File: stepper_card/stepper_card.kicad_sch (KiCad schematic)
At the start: 19 parts, among them J1 Bus_PCI_Express_x1, J2 Conn_01x04, SW1 SW_DIP_x04, U1 DRV8825PWPR_Stepper_Driver

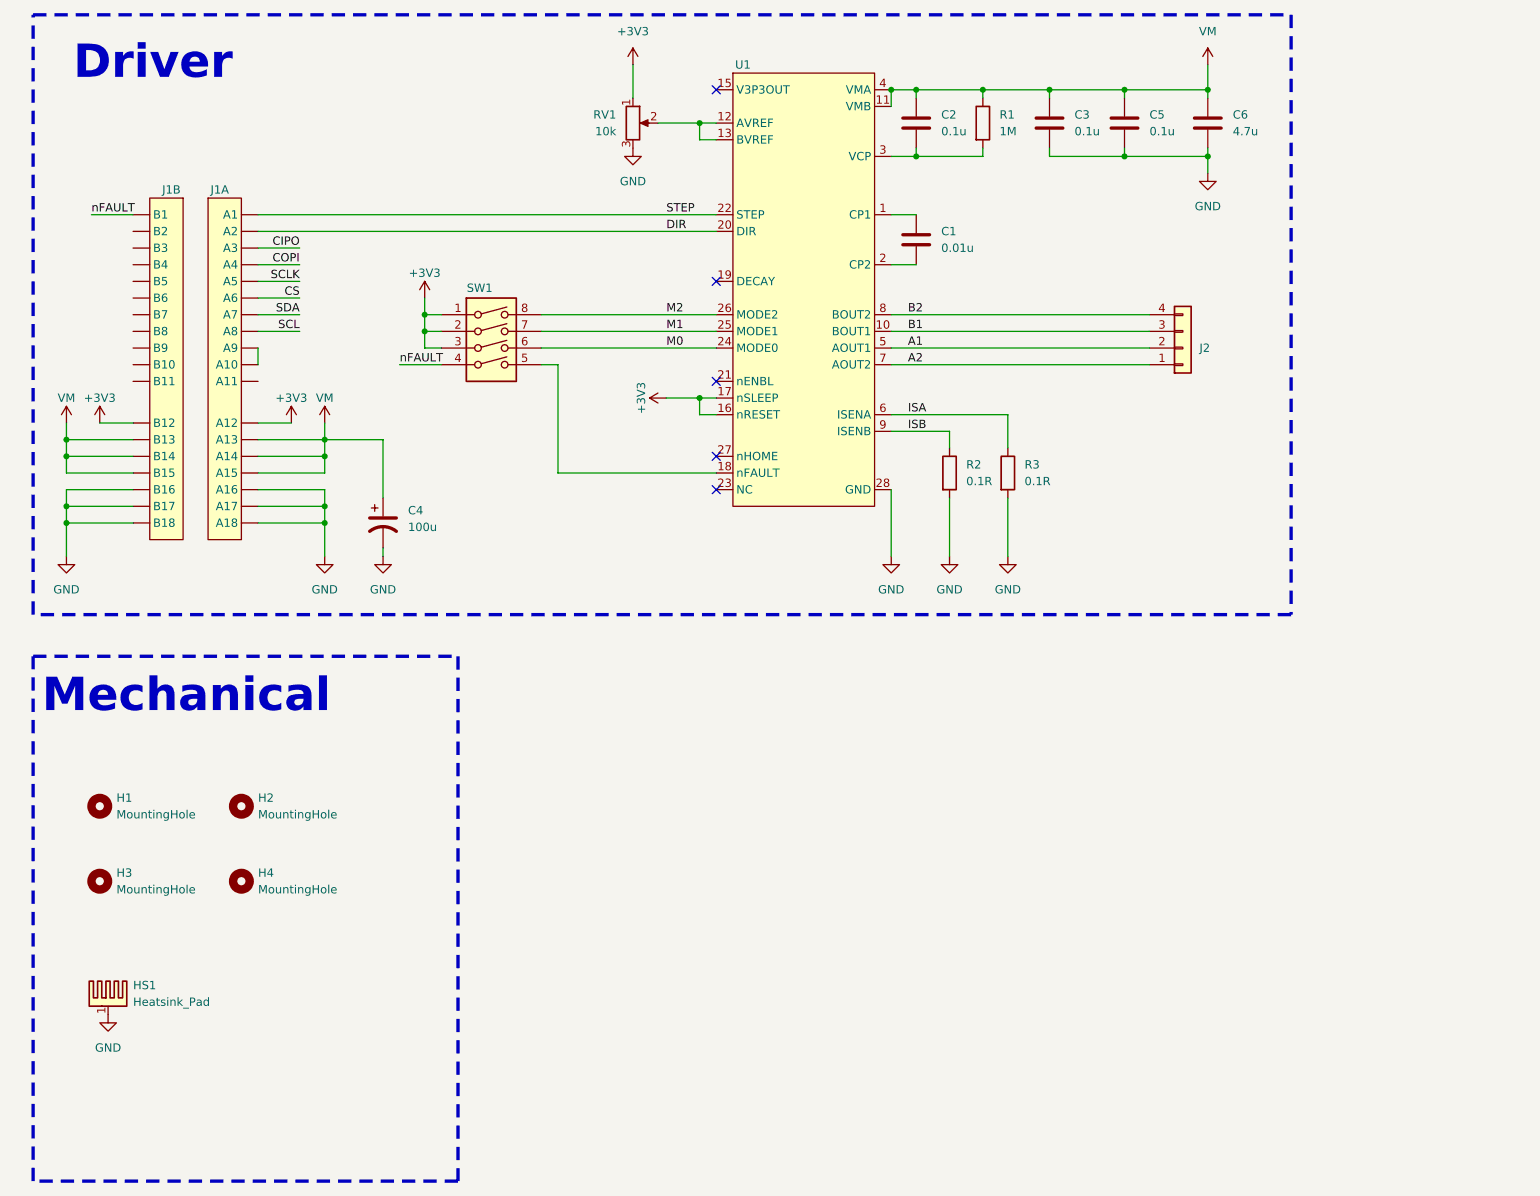
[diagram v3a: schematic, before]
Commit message: finished routing added test points
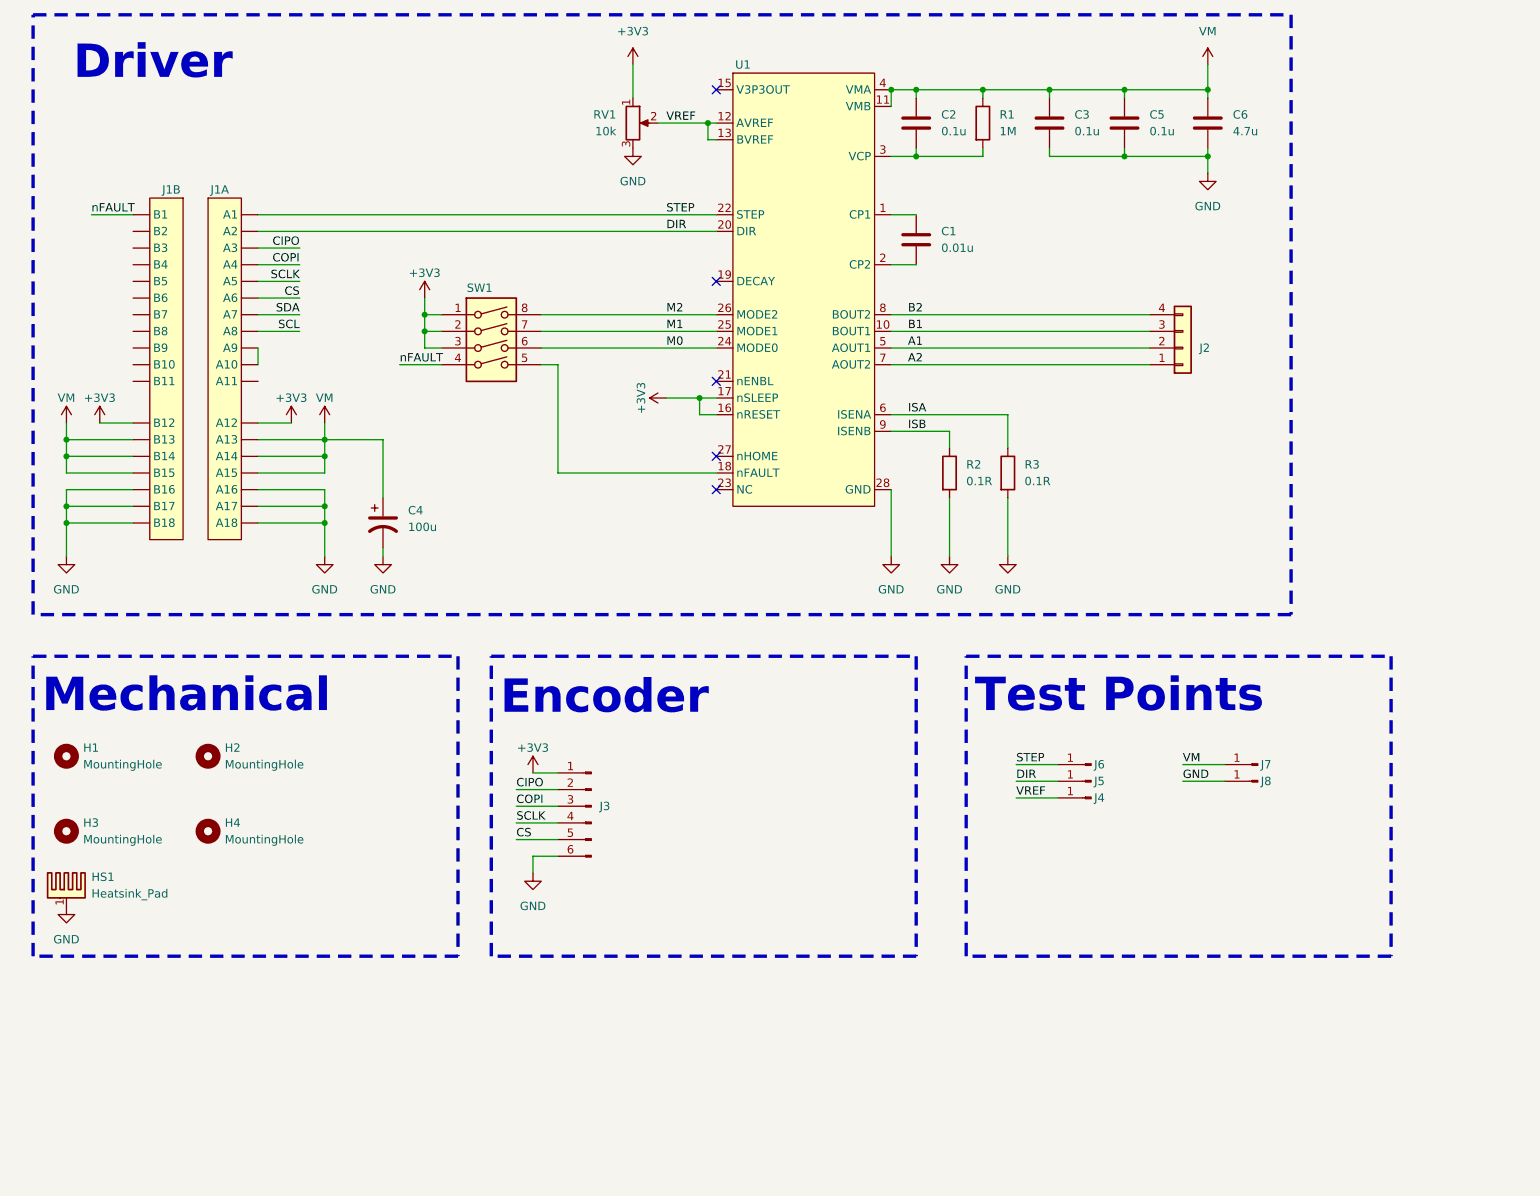
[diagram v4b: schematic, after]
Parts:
- added J3: Conn_01x06_Pin, Connector_PinHeader_2.54mm:PinHeader_1x06_P2.54mm_Horizontal, symbol Connector:Conn_01x06_Pin
- added J4, J5, J6, J7, J8: Conn_01x01_Pin, TestPoint:TestPoint_Pad_2.0x2.0mm, symbol Connector:Conn_01x01_Pin
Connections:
- net +3V3: now also J3.1 (Pin_1)
- net CIPO: now also J3.2 (Pin_2)
- net COPI: now also J3.3 (Pin_3)
- net CS: now also J3.5 (Pin_5)
- net DIR: now also J5.1 (Pin_1)
- net GND: now also J3.6 (Pin_6), J8.1 (Pin_1)
- net SCLK: now also J3.4 (Pin_4)
- net STEP: now also J6.1 (Pin_1)
- net VM: now also J7.1 (Pin_1)
- net VREF: now reaches RV1.2, U1.12 (AVREF), U1.13 (BVREF)
- net VREF: now also J4.1 (Pin_1)
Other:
- note added: "Encoder"
- note added: "Test Points"
- moved on the sheet: H1, H2, H3, H4, HS1
